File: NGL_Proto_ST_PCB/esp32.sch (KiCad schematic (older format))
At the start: 21 parts, among them J2 Conn_01x04_Male, J4 Conn_01x06_Male, J5 Conn_01x04_Male, J6 Conn_01x03_Male, SW3 SW_Push, SW4 SW_Push, U4 ESP32-WROOM-32D-N16, U9 MCP3426A0-E_SN

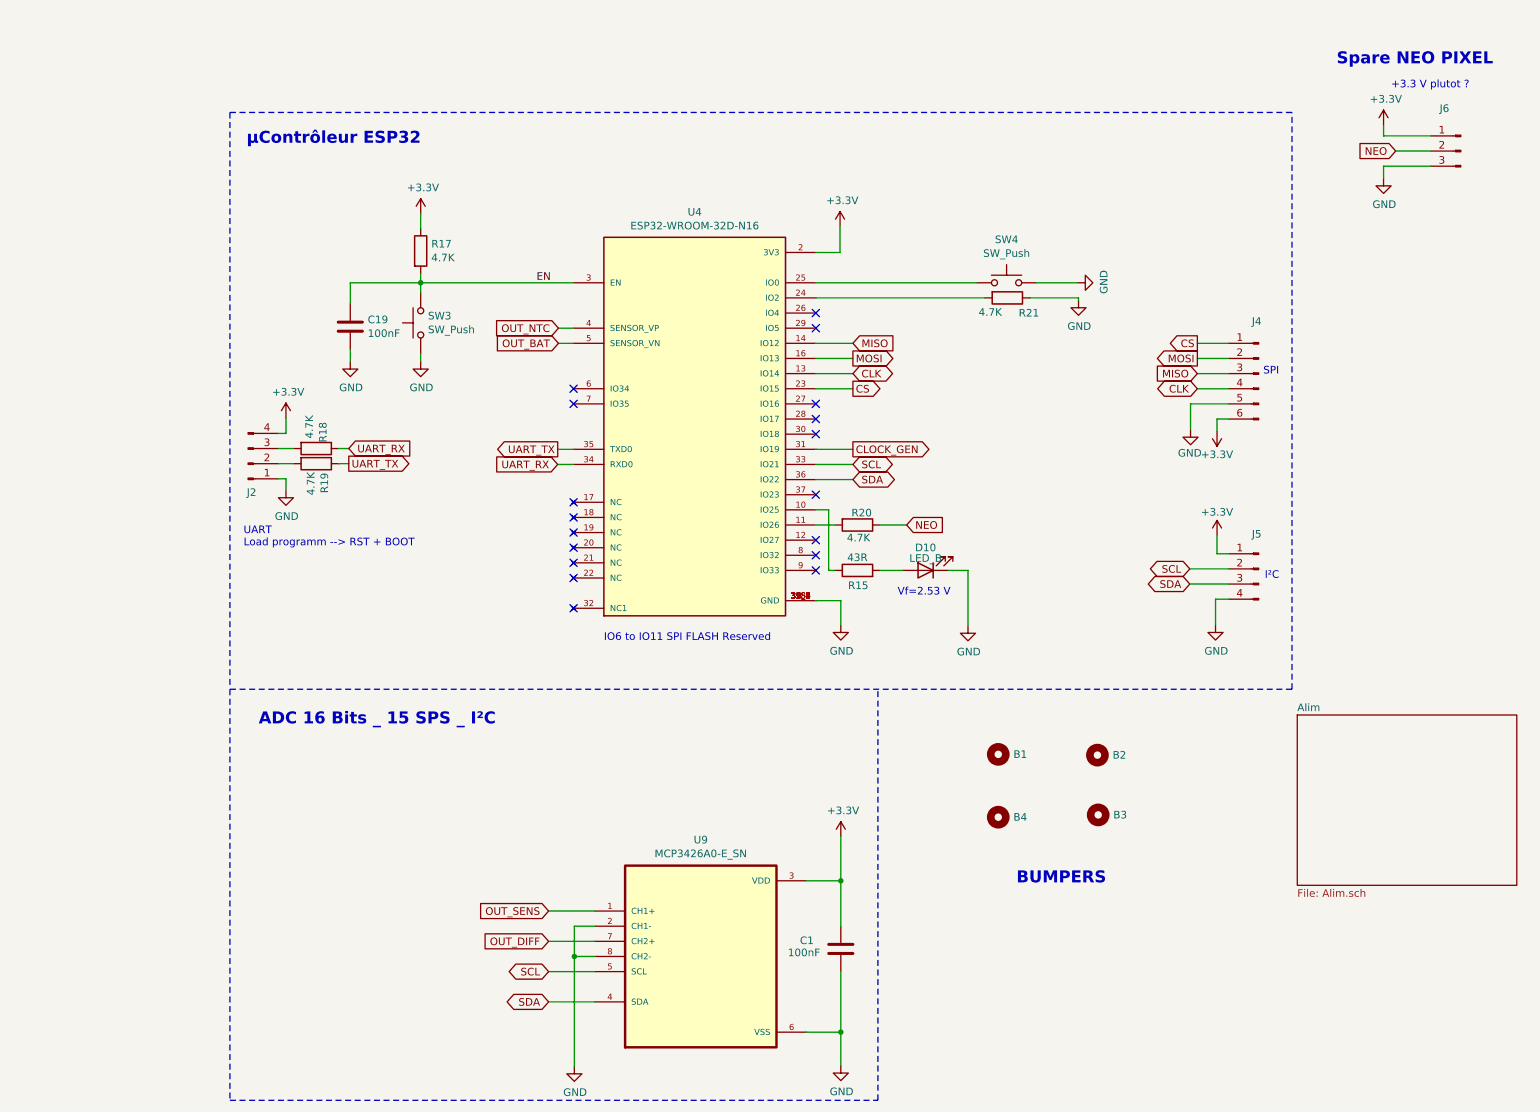
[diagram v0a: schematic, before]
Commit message: Rrecherche sur pot num et mise en page
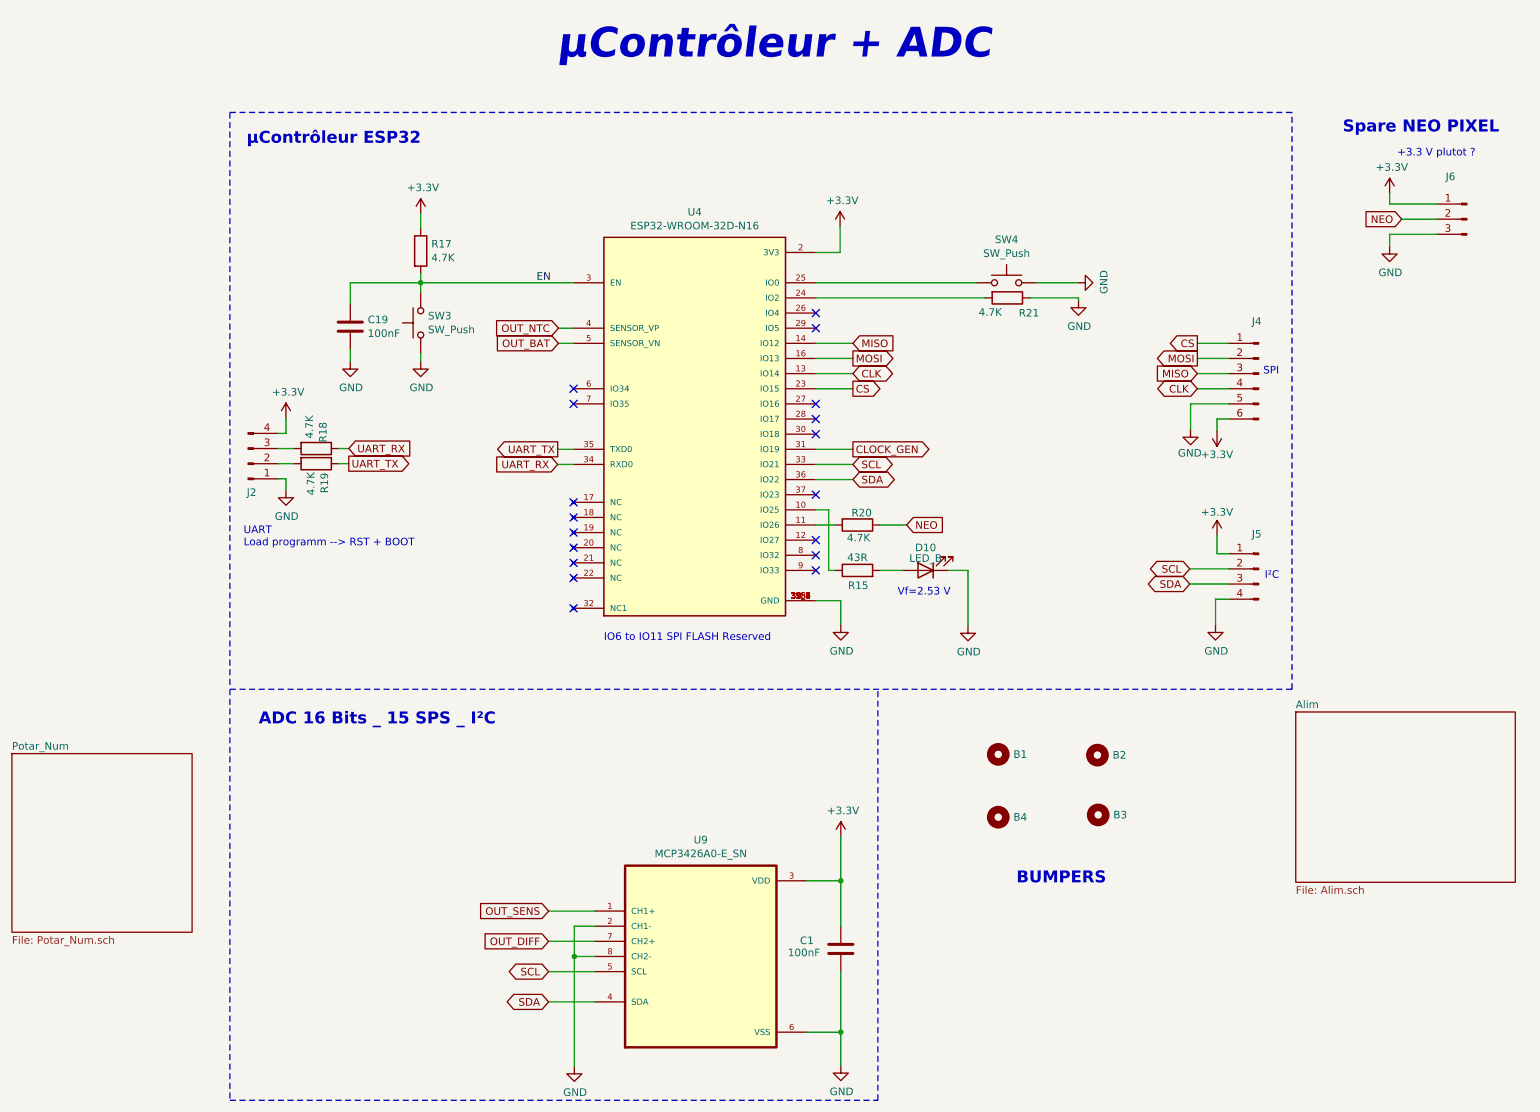
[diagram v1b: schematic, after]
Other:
- note added: "μContrôleur + ADC"
- moved on the sheet: J6
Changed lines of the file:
@@
 $Descr A4 11693 8268
 encoding utf-8
-Sheet 2 5
-Title "NGL_Proto"
-Date "2022-05-02"
-Rev "V1"
+Sheet 2 6
+Title "NGL_Proto_V2"
+Date "2022-05-27"
+Rev "V2"
 Comp "ADTP"
-Comment1 "Usinage by LPKF"
-Comment2 ""
-Comment3 ""
+Comment1 "Auteur: Benoît"
+Comment2 "Proto avec potar numérique + intégration"
+Comment3 "Sous traité chez JLCPCB"
 Comment4 ""
 $EndDescr
@@
 $EndComp
 $Sheet
-S 9550 5195 1450 1125
+S 9540 5175 1450 1125
 U 62744FDF
 F0 "Alim" 50
@@
 L Connector:Conn_01x03_Male J6
 U 1 1 62749F36
-P 10630 1470
-F 0 "J6" H 10738 1751 50  0000 C CNN
-F 1 "Conn_01x03_Male" H 10738 1660 50  0001 C CNN
-F 2 "Connector_PinHeader_2.54mm:PinHeader_1x03_P2.54mm_Vertical" H 10630 1470 50  0001 C CNN
-F 3 "~" H 10630 1470 50  0001 C CNN
-	1    10630 1470
+P 10670 1920
+F 0 "J6" H 10778 2201 50  0000 C CNN
+F 1 "Conn_01x03_Male" H 10778 2110 50  0001 C CNN
+F 2 "Connector_PinHeader_2.54mm:PinHeader_1x03_P2.54mm_Vertical" H 10670 1920 50  0001 C CNN
+F 3 "~" H 10670 1920 50  0001 C CNN
+	1    10670 1920
 	-1   0    0    -1
 $EndComp
@@
 L power:GND #PWR048
 U 1 1 6274CE22
-P 10120 1650
-F 0 "#PWR048" H 10120 1400 50  0001 C CNN
-F 1 "GND" H 10125 1477 50  0000 C CNN
-F 2 "" H 10120 1650 50  0001 C CNN
-F 3 "" H 10120 1650 50  0001 C CNN
-	1    10120 1650
+P 10160 2100
+F 0 "#PWR048" H 10160 1850 50  0001 C CNN
+F 1 "GND" H 10165 1927 50  0000 C CNN
+F 2 "" H 10160 2100 50  0001 C CNN
+F 3 "" H 10160 2100 50  0001 C CNN
+	1    10160 2100
 	1    0    0    -1
 $EndComp
 Text GLabel 6970 3940 2    50   Input ~ 0
 NEO
-Text GLabel 10200 1470 0    50   Input ~ 0
+Text GLabel 10240 1920 0    50   Input ~ 0
 NEO
 $Comp
@@
 	6495 3940 6370 3940
 Wire Wire Line
-	10430 1370 10120 1370
-Wire Wire Line
-	10430 1470 10200 1470
-Wire Wire Line
-	10430 1570 10120 1570
+	10470 1820 10160 1820
+Wire Wire Line
+	10470 1920 10240 1920
+Wire Wire Line
+	10470 2020 10160 2020
 Wire Wire Line
 	3760 2340 3295 2340
@@
 Text Notes 2610 1435 0    79   ~ 16
 μContrôleur ESP32
-Text Notes 9810 910  0    79   ~ 16
+Text Notes 9850 1360 0    79   ~ 16
 Spare NEO PIXEL
 NoConn ~ 6370 2540
@@
 NoConn ~ 4770 3040
 Wire Wire Line
-	10120 1570 10120 1650
+	10160 2020 10160 2100
 Text GLabel 4670 2740 0    50   Input ~ 0
 OUT_BAT
@@
 Wire Wire Line
 	8845 3140 8845 3310
-Text Notes 10170 1065 0    50   ~ 0
+Text Notes 10210 1515 0    50   ~ 0
 +3.3 V plutot ?
 Wire Notes Line
@@
 L power:+3.3V #PWR0115
 U 1 1 6297253D
-P 10120 1300
-F 0 "#PWR0115" H 10120 1150 50  0001 C CNN
-F 1 "+3.3V" H 10135 1473 50  0000 C CNN
-F 2 "" H 10120 1300 50  0001 C CNN
-F 3 "" H 10120 1300 50  0001 C CNN
-	1    10120 1300
-	1    0    0    -1
-$EndComp
-Wire Wire Line
-	10120 1300 10120 1370
+P 10160 1750
+F 0 "#PWR0115" H 10160 1600 50  0001 C CNN
+F 1 "+3.3V" H 10175 1923 50  0000 C CNN
+F 2 "" H 10160 1750 50  0001 C CNN
+F 3 "" H 10160 1750 50  0001 C CNN
+	1    10160 1750
+	1    0    0    -1
+$EndComp
+Wire Wire Line
+	10160 1750 10160 1820
 Wire Wire Line
 	6795 3940 6970 3940
@@
 EN
 $Comp
-L power:+3.3V #PWR?
+L power:+3.3V #PWR0114
 U 1 1 6291663C
 P 9020 4010
-F 0 "#PWR?" H 9020 3860 50  0001 C CNN
+F 0 "#PWR0114" H 9020 3860 50  0001 C CNN
 F 1 "+3.3V" H 9020 4165 50  0000 C CNN
 F 2 "" H 9020 4010 50  0001 C CNN
@@
 Wire Wire Line
 	9020 4130 9020 4010
+$Sheet
+S 1060 5450 1190 1180
+U 629412F2
+F0 "Potar_Num" 50
+F1 "Potar_Num.sch" 50
+$EndSheet
+Text Notes 4660 880  0    197  Italic 39
+μContrôleur + ADC
 $EndSCHEMATC

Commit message: Ajuut nouveaux composants: commande 3
Attente question ENABL E + POTAR
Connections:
- net CS: no longer U4.23 (IO15)
- net CS_R10: now reaches U4.27 (IO16)
- net CS_R2: now reaches U4.28 (IO17)
- net MOTEUR: now reaches U4.30 (IO18)
- no-connect marks 18 -> 15
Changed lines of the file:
@@
 NoConn ~ 6370 2540
 NoConn ~ 6370 2640
-NoConn ~ 6370 3140
-NoConn ~ 6370 3240
-NoConn ~ 6370 3340
 $Comp
 L MCP3426A0-E_SN:MCP3426A0-E_SN U9
@@
 Text GLabel 6615 2940 2    50   BiDi ~ 0
 CLK
-Text GLabel 6615 3040 2    50   Output ~ 0
-CS
-Wire Wire Line
-	6615 3040 6370 3040
 Wire Wire Line
 	6615 2940 6370 2940
@@
 Text Notes 4660 880  0    197  Italic 39
 μContrôleur + ADC
+Text GLabel 6615 3140 2    50   Output ~ 0
+CS_R10
+Text GLabel 6615 3240 2    50   Output ~ 0
+CS_R2
+Wire Wire Line
+	6615 3140 6370 3140
+Wire Wire Line
+	6615 3240 6370 3240
+Text GLabel 6615 3340 2    50   Output ~ 0
+MOTEUR
+Wire Wire Line
+	6615 3340 6370 3340
 $EndSCHEMATC

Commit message: Avancement après réunion mercredi
finir pour mettre en review puis attente.
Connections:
- no-connect marks 15 -> 16
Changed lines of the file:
@@
 Wire Wire Line
 	6615 3340 6370 3340
+NoConn ~ 6370 3040
 $EndSCHEMATC

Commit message: Commit avant DSN
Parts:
- removed R18, R19: 4.7K, Resistor_SMD:R_0805_2012Metric, symbol Device:R
- C1, C19: footprint Capacitor_SMD:C_0805_2012Metric -> Capacitor_SMD:C_0805_2012Metric_Pad1.18x1.45mm_HandSolder
- R15, R17, R20, R21: footprint Resistor_SMD:R_0805_2012Metric -> Resistor_SMD:R_0805_2012Metric_Pad1.20x1.40mm_HandSolder
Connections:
- net CS is gone; now on net CS_R2: J4.1 (Pin_1)
- net UART_RX: now also J2.3 (Pin_3)
- net UART_TX: now also J2.2 (Pin_2)
- net INH: now reaches U4.37 (IO23)
- no-connect marks 16 -> 15
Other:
- note added: "*INT sur petit coté"
- note added: "*Pull-up Interne"
- note added: "Entrée ENABLE pooling"
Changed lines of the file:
@@
 encoding utf-8
 Sheet 2 6
-Title "NGL_Proto_V2"
-Date "2022-05-27"
-Rev "V2"
+Title "NGL_Proto_ST"
+Date "2022-06-09"
+Rev "V1.1"
 Comp "ADTP"
 Comment1 "Auteur: Benoît"
@@
 F 0 "R15" V 6545 4235 50  0000 C CNN
 F 1 "43R" V 6730 4240 50  0000 C CNN
-F 2 "Resistor_SMD:R_0805_2012Metric" V 6575 4240 50  0001 C CNN
+F 2 "Resistor_SMD:R_0805_2012Metric_Pad1.20x1.40mm_HandSolder" V 6575 4240 50  0001 C CNN
 F 3 "~" H 6645 4240 50  0001 C CNN
 	1    6645 4240
@@
 F 0 "R17" H 3830 2176 50  0000 L CNN
 F 1 "4.7K" H 3830 2085 50  0000 L CNN
-F 2 "Resistor_SMD:R_0805_2012Metric" V 3690 2130 50  0001 C CNN
+F 2 "Resistor_SMD:R_0805_2012Metric_Pad1.20x1.40mm_HandSolder" V 3690 2130 50  0001 C CNN
 F 3 "~" H 3760 2130 50  0001 C CNN
 	1    3760 2130
@@
 F 0 "R21" V 7735 2515 50  0000 L CNN
 F 1 "4.7K" V 7730 2250 50  0000 L CNN
-F 2 "Resistor_SMD:R_0805_2012Metric" V 7565 2440 50  0001 C CNN
+F 2 "Resistor_SMD:R_0805_2012Metric_Pad1.20x1.40mm_HandSolder" V 7565 2440 50  0001 C CNN
 F 3 "~" H 7635 2440 50  0001 C CNN
 	1    7635 2440
@@
 $EndComp
 $Comp
-L Device:R R18
-U 1 1 627449C1
-P 3070 3435
-F 0 "R18" H 2895 3480 50  0000 L CNN
-F 1 "4.7K" H 2850 3390 50  0000 L CNN
-F 2 "Resistor_SMD:R_0805_2012Metric" V 3000 3435 50  0001 C CNN
-F 3 "~" H 3070 3435 50  0001 C CNN
-	1    3070 3435
-	0    1    1    0
-$EndComp
-$Comp
-L Device:R R19
-U 1 1 62746645
-P 3070 3535
-F 0 "R19" H 3130 3590 50  0000 L CNN
-F 1 "4.7K" H 3125 3500 50  0000 L CNN
-F 2 "Resistor_SMD:R_0805_2012Metric" V 3000 3535 50  0001 C CNN
-F 3 "~" H 3070 3535 50  0001 C CNN
-	1    3070 3535
-	0    1    1    0
-$EndComp
-$Comp
 L power:+3.3V #PWR025
 U 1 1 62747B61
@@
 F 0 "R20" V 6565 3900 50  0000 L CNN
 F 1 "4.7K" V 6730 3870 50  0000 L CNN
-F 2 "Resistor_SMD:R_0805_2012Metric" V 6575 3940 50  0001 C CNN
+F 2 "Resistor_SMD:R_0805_2012Metric_Pad1.20x1.40mm_HandSolder" V 6575 3940 50  0001 C CNN
 F 3 "~" H 6645 3940 50  0001 C CNN
 	1    6645 3940
@@
 F 0 "C19" H 3410 2676 50  0000 L CNN
 F 1 "100nF" H 3410 2585 50  0000 L CNN
-F 2 "Capacitor_SMD:C_0805_2012Metric" H 3333 2480 50  0001 C CNN
+F 2 "Capacitor_SMD:C_0805_2012Metric_Pad1.18x1.45mm_HandSolder" H 3333 2480 50  0001 C CNN
 F 3 "~" H 3295 2630 50  0001 C CNN
 	1    3295 2630
@@
 Wire Wire Line
 	3760 2860 3760 2805
-Wire Wire Line
-	2920 3535 2820 3535
-Wire Wire Line
-	2920 3435 2820 3435
 Wire Wire Line
 	2820 3335 2870 3335
@@
 Text Notes 2690 5270 0    79   ~ 16
 ADC 16 Bits _ 15 SPS _ I²C
-NoConn ~ 6370 3740
 NoConn ~ 6370 4040
 NoConn ~ 6370 4140
@@
 F 0 "C1" H 6265 6795 50  0000 L CNN
 F 1 "100nF" H 6185 6715 50  0000 L CNN
-F 2 "Capacitor_SMD:C_0805_2012Metric" H 6573 6590 50  0001 C CNN
+F 2 "Capacitor_SMD:C_0805_2012Metric_Pad1.18x1.45mm_HandSolder" H 6573 6590 50  0001 C CNN
 F 3 "~" H 6535 6740 50  0001 C CNN
 	1    6535 6740
@@
 Text GLabel 3285 3435 2    50   Input ~ 0
 UART_RX
-Wire Wire Line
-	3285 3435 3220 3435
-Wire Wire Line
-	3220 3535 3285 3535
 $Comp
 L Connector:Conn_01x06_Male J4
@@
 	9095 2940 8890 2940
 Text GLabel 8890 2740 0    50   Output ~ 0
-CS
+CS_R2
 Wire Wire Line
 	9095 3040 8890 3040
@@
 	6615 3340 6370 3340
 NoConn ~ 6370 3040
+Wire Wire Line
+	2820 3435 3285 3435
+Wire Wire Line
+	2820 3535 3285 3535
+Text Notes 7960 4300 0    50   ~ 0
+*Pull-up Interne
+Text Notes 1555 2340 0    50   ~ 0
+*INT sur petit coté
+Text GLabel 6620 3740 2    50   Input ~ 0
+INH
+Wire Wire Line
+	6620 3740 6370 3740
+Text Notes 6875 3775 0    50   ~ 0
+Entrée ENABLE pooling
 $EndSCHEMATC
